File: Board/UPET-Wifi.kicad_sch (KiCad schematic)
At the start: 22 parts, among them J1 Conn_01x06, J3 Conn_01x09, Q1 S8050, Q2 S8050, U1 ESP32-C3-WROOM-02, U2 SC16IS752IPW, U3 1.8432 MHz

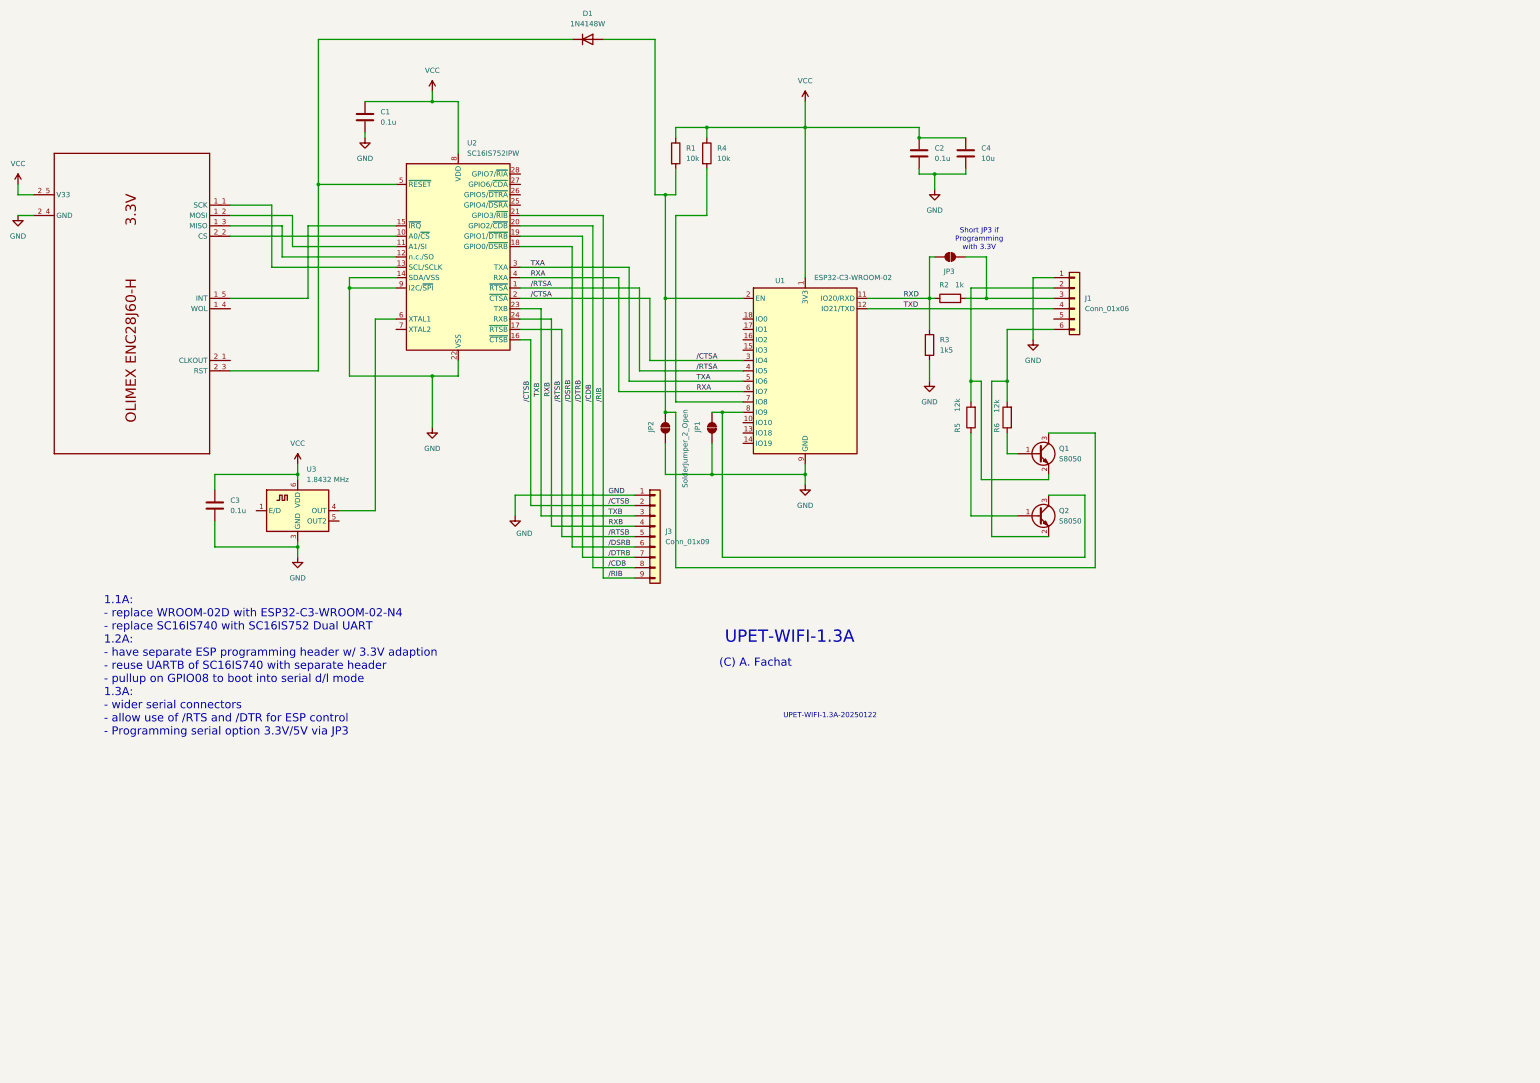
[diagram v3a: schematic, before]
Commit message: replace ESP32-WROOM with an ESP32-VROVER-E
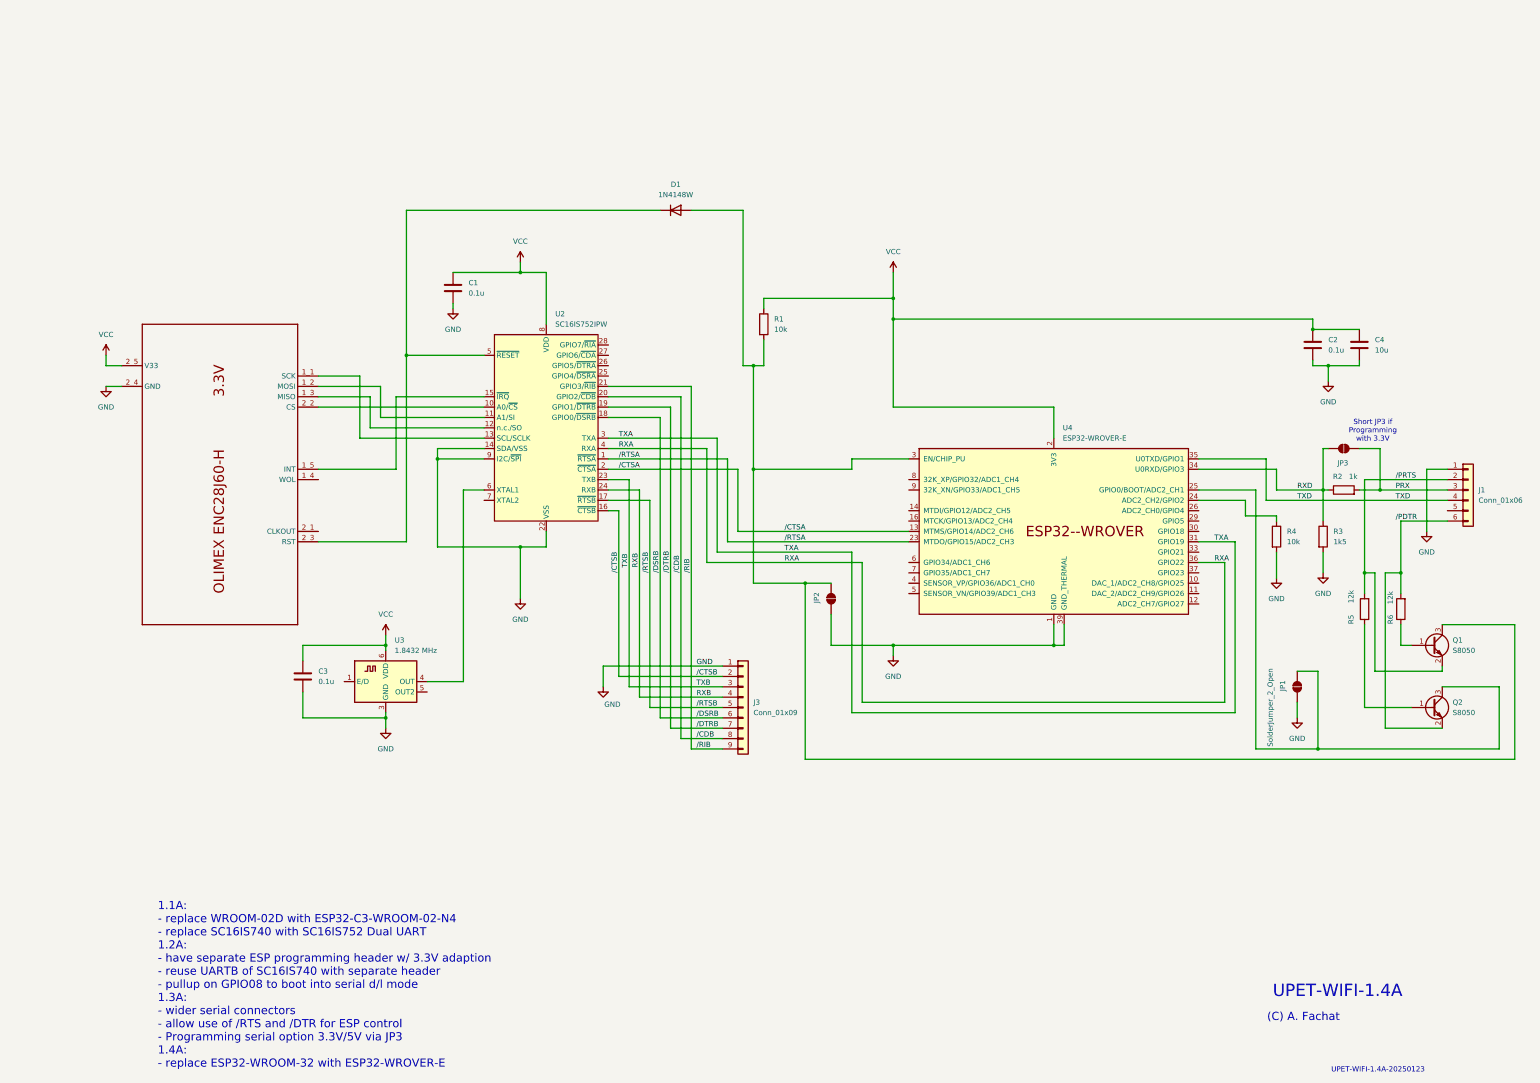
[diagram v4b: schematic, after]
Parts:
- removed U1: ESP32-C3-WROOM-02, RF_Module:ESP32-C3-WROOM-02, symbol RF_Module:ESP32-C3-WROOM-02
- added U4: ESP32-WROVER-E, PCM_Espressif:ESP32-WROVER-E, symbol PCM_Espressif:ESP32-WROVER-E
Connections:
- net GND: now also R4.2, U4.1 (GND), U4.15 (GND), U4.38 (GND), U4.39 (GND_THERMAL)
- net RXA: now also U4.36 (GPIO22)
- net RXD: now also U4.34 (U0RXD/GPIO3)
- net TXA: now also U4.31 (GPIO19)
- net TXD: now also U4.35 (U0TXD/GPIO1)
- net VCC: now also U4.2 (3V3); no longer R4.1
- net /CTSA: now also U4.13 (MTMS/GPIO14/ADC2_CH6)
- net /RTSA: now also U4.23 (MTDO/GPIO15/ADC2_CH3)
- net at D1.2 (A), JP2.2 (B), Q1.3 (C)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: now also U4.3 (EN/CHIP_PU)
- net at JP1.2 (B), Q2.3 (C): now also U4.25 (GPIO0/BOOT/ADC2_CH1)
- net /PRTS: now reaches J1.2 (Pin_2), Q1.2 (E), R5.2
- net PRX: now reaches J1.3 (Pin_3), JP3.1 (A), R2.2
- new net: R4.1, U4.24 (ADC2_CH2/GPIO2)
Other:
- note added: "1.1A: - replace WROOM-02D with ESP32-C3-WROOM-02-N4 - replace SC16IS740 with SC16IS752 Dual UART 1.2A: - have separate ESP programming header w/ 3.3V adaption - reuse UARTB of SC16IS740 with separate header - pullup on GPIO08 to boot into serial d/l mode 1.3A: - wider serial connectors - allow use of /RTS and /DTR for ESP control - Programming serial option 3.3V/5V via JP3 1.4A: - replace ESP32-W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"
- note added: "UPET-WIFI-1.4A"
- note added: "UPET-WIFI-1.4A-20250123"
- note removed: "1.1A: - replace WROOM-02D with ESP32-C3-WROOM-02-N4 - replace SC16IS740 with SC16IS752 Dual UART 1.2A: - have separate ESP programming header w/ 3.3V adaption - reuse UARTB of SC16IS740 with separate header - pullup on GPIO08 to boot into serial d/l mode 1.3A: - wider serial connectors - allow use of /RTS and /DTR for ESP control - Programming serial option 3.3V/5V via JP3"
- note removed: "UPET-WIFI-1.3A"
- note removed: "UPET-WIFI-1.3A-20250122"
- moved on the sheet: C1, C2, C3, C4, D1, J1, J3, JP1, JP2, JP3, Q1, Q2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
